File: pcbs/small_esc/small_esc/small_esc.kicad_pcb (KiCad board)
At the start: 2 copper layers, 120 x 90 mm, 48 parts, among them J1 Conn_01x04_Female, J2 Conn_01x13_Female, J3 Conn_01x10_Female, J4 Conn_01x03_Female, SW1 load iar, SW10 1, SW11 2, SW12 3, SW13 4, SW14 5, SW15 6, SW16 7, SW17 8, SW18 9, SW19 0, SW2 load addr, SW20 A, SW21 B, SW22 C, SW23 ki reset, SW24 run, SW25 stop, SW26 dump, SW27 check, SW28 reload, SW3 load store, SW4 decr addr, SW5 incr addr, SW6 normal reset, SW7 clear, SW8 minus, SW9 point, U1 Pico, U2 AP1117-33

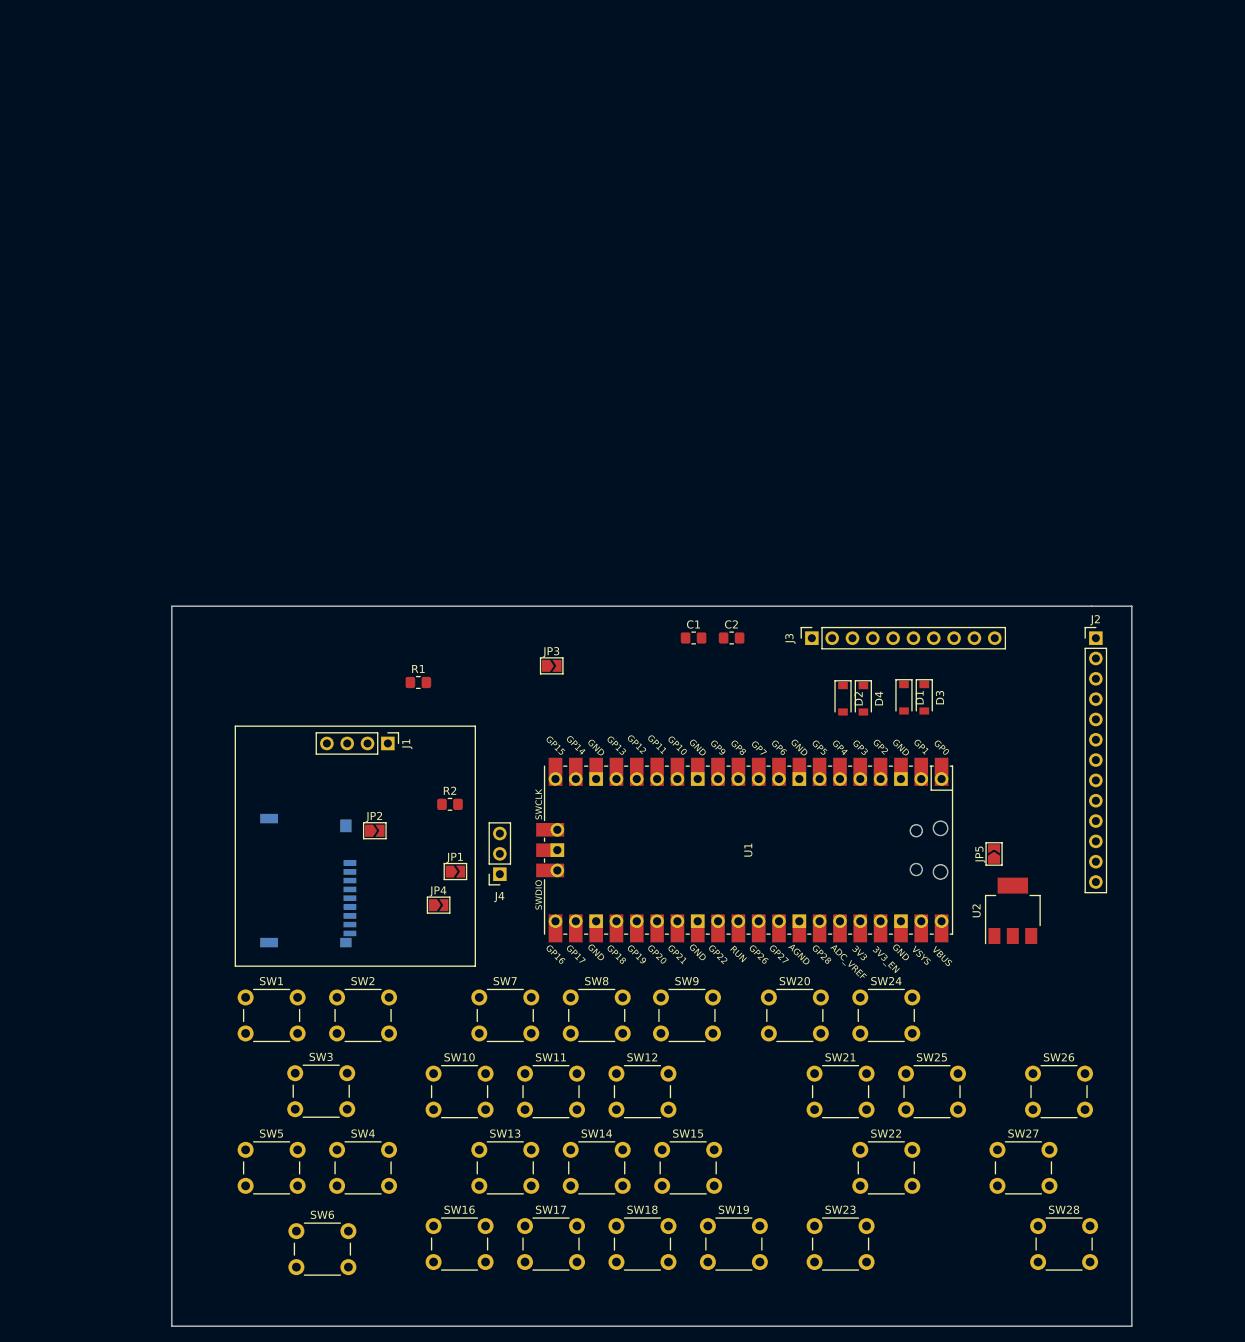
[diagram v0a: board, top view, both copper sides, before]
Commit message: Added PCB artwork for V1.0 small PCb version. Pico, small keyboard and a 0.96" OLED screen. Options for mounting screen and powering the board. GPIOs run to connectors so external keyboard and display an option. SD card slot for code storage/cassette emulation.
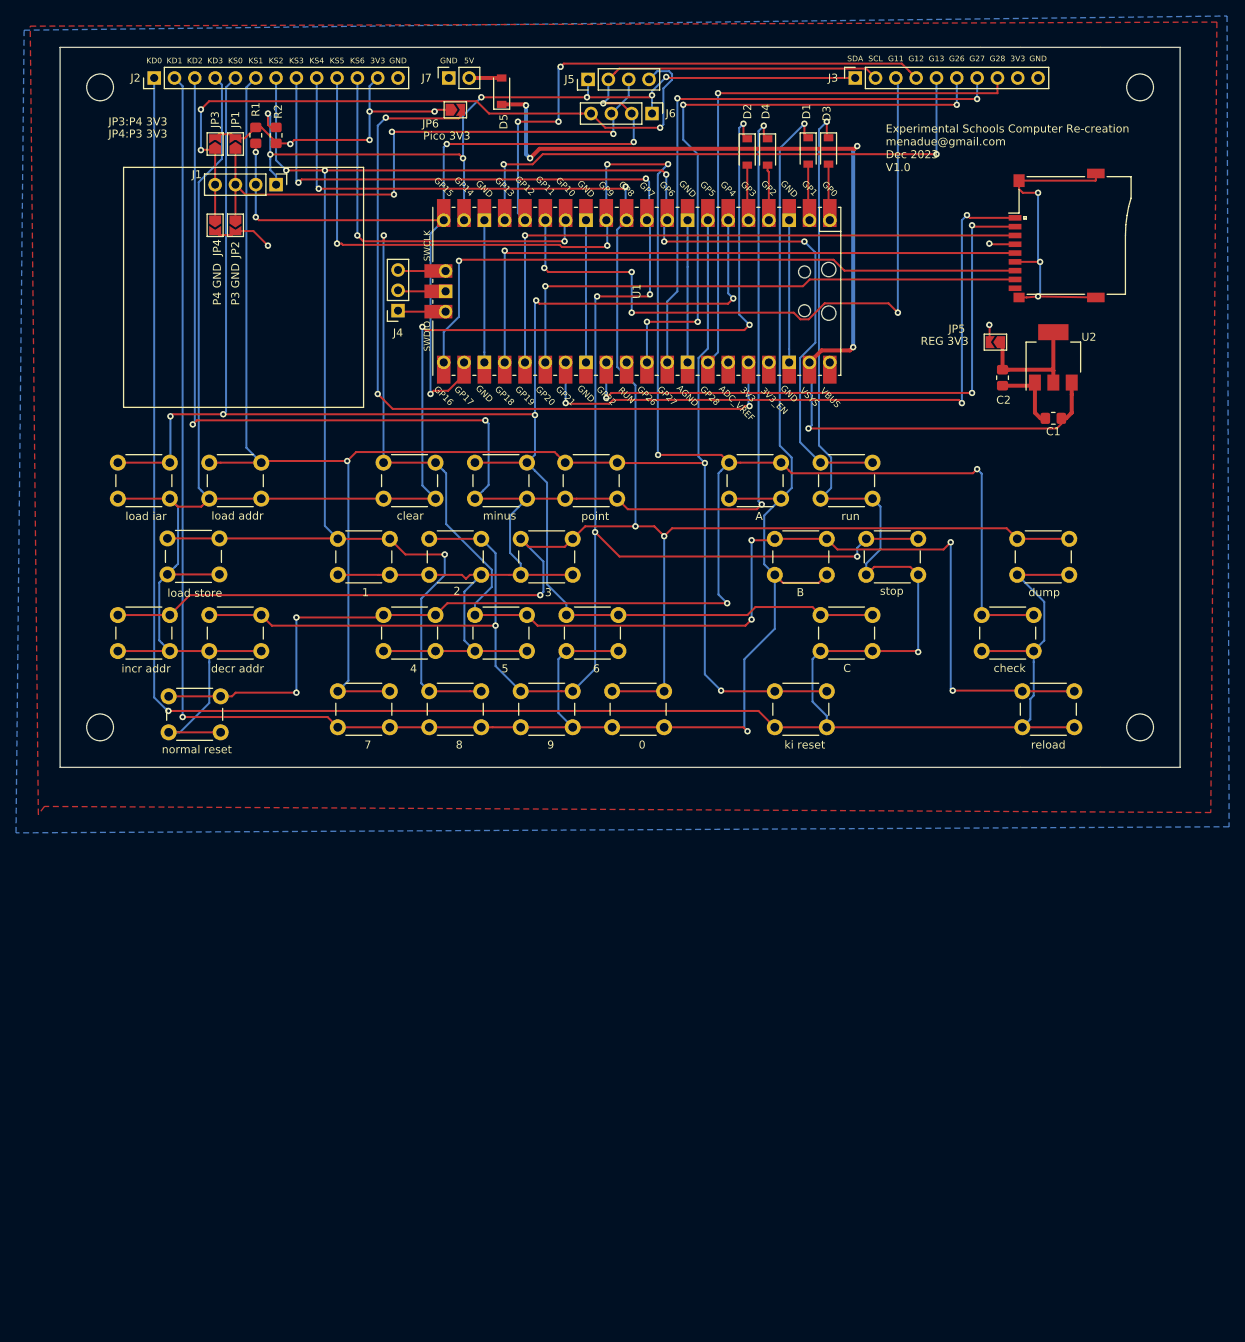
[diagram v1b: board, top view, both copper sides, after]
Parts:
- added D5: SS36, Diode_SMD:D_SOD-123, F.Cu at (141.2, 55.6)
- added J5: Conn_01x04_Female, Connector_PinHeader_2.54mm:PinHeader_1x04_P2.54mm_Vertical, F.Cu at (152.0, 54.1)
- added J6: Conn_01x04_Female, Connector_PinHeader_2.54mm:PinHeader_1x04_P2.54mm_Vertical, F.Cu at (160.0, 58.4)
- added J7: Conn_01x02_Female, Connector_PinSocket_2.54mm:PinSocket_1x02_P2.54mm_Vertical, F.Cu at (134.6, 54.0)
- added JP6: Jumper_NO_Small, Jumper:SolderJumper-2_P1.3mm_Open_TrianglePad1.0x1.5mm, F.Cu at (135.4, 58.0)
- C1, C2: value C_Small -> 100nF
- JP1: value Jumper_NO_Small -> Pin3 3V3
- JP2: value Jumper_NO_Small -> Pin3 GND
- JP3: value Jumper_NO_Small -> Pin4 3V3
- JP4: value Jumper_NO_Small -> Pin4 GND
- XS1: moved to F.Cu
- moved J2 137.0 mm to (97.8, 54.0), turned to 90 degrees
- moved XS1 131.7 mm to (215.9, 73.7)
- moved JP1 95.0 mm to (108.0, 62.2), turned to 90 degrees
- moved JP4 89.5 mm to (105.4, 72.4), turned to 270 degrees
- moved R2 87.1 mm to (110.5, 61.1), turned to 270 degrees
- moved JP2 77.7 mm to (108.0, 72.4), turned to 270 degrees
- moved JP3 77.6 mm to (105.4, 62.2), turned to 90 degrees
- moved J4 71.6 mm to (128.3, 83.1)
- moved U1 71.2 mm to (158.1, 80.6)
- moved J1 71.2 mm to (113.0, 67.3)
- moved R1 70.7 mm to (113.0, 61.1), turned to 90 degrees
- moved J3 70.2 mm to (185.4, 54.0)
- moved D1 69.4 mm to (179.5, 63.1)
- moved D2 69.4 mm to (171.9, 63.2)
- moved D3 69.4 mm to (182.1, 63.1)
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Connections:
- net Net-(J1-Pad3) renamed OLED_P3
- net Net-(J1-Pad4) renamed OLED_P4
- C1 pad 1: VBUS -> VSYS
- J3 pad 3: (no net) -> GPIO11
- J3 pad 4: (no net) -> GPIO12
- J3 pad 5: (no net) -> GPIO13
- U1 pad 36: +3V3 -> Net-(JP6-Pad2)
- U1 pad 39: Net-(U1-Pad39) -> VSYS
- U1 pad 40: VBUS -> Net-(U1-Pad40)
- U2 pad 3: VBUS -> VSYS
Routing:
- net KBD_DRV_0: track 0.00 -> 336.5 mm, vias 0 -> 3
- net KBD_SENSE_5: track 0.00 -> 274.2 mm, vias 0 -> 9
- net KBD_DRV_1: track 0.00 -> 266.2 mm, vias 0 -> 3
- net KBD_SENSE_4: track 0.00 -> 256.0 mm, vias 0 -> 5
- net KBD_DRV_3: track 0.00 -> 251.7 mm, vias 0 -> 3
- net KBD_DRV_2: track 0.00 -> 246.7 mm, vias 0 -> 4
- net KBD_SENSE_3: track 0.00 -> 242.7 mm, vias 0 -> 7
- net KBD_SENSE_2: track 0.00 -> 229.9 mm, vias 0 -> 6
- net KBD_SENSE_0: track 0.00 -> 223.3 mm, vias 0 -> 5
- net KBD_SENSE_1: track 0.00 -> 222.0 mm, vias 0 -> 3
- net KBD_SENSE_6: track 0.00 -> 212.2 mm, vias 0 -> 7
- net I2C_SCLK: track 0.00 -> 140.6 mm, vias 0 -> 6
- net VSYS: track 0.00 -> 129.5 mm, vias 0 -> 5
- net GND: track 0.00 -> 128.5 mm, vias 0 -> 4
- net I2C_SDA: track 0.00 -> 105.2 mm, vias 0 -> 7
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- added copper zone on B.Cu, net +3V3
- added copper zone on F.Cu, net GND
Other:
- board size 120 x 90 mm -> 140 x 90 mm
- board text added: "3V3"
- board text added: "5V"
- board text added: "Experimental Schools Computer Re-creation menadue@gmail.com Dec 2023 V1.0"
- board text added: "G11"
- board text added: "G12"
- board text added: "G13"
- board text added: "G26"
- board text added: "G27"
- board text added: "G28"
- board text added: "GND"
- board text added: "JP3:P4 3V3"
- board text added: "JP4:P3 3V3"
- board text added: "KD0"
- board text added: "KD1"
- board text added: "KD2"
- board text added: "KD3"
- board text added: "KS0"
- board text added: "KS1"
- board text added: "KS2"
- board text added: "KS3"
- board text added: "KS4"
- board text added: "KS5"
- board text added: "KS6"
- board text added: "P3 GND"
- board text added: "P4 GND"
- board text added: "Pico 3V3"
- board text added: "REG 3V3"
- board text added: "SCL"
- board text added: "SDA"
